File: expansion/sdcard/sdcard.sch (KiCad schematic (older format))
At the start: 26 parts, among them J1 Conn_01x08, J2 Conn_01x10, J3 SD_Card, Q1 2N7002, Q2 2N7002, Q3 2N7002, Q4 2N7002, Q5 2N7002, Q6 2N7002, U1 74HC574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

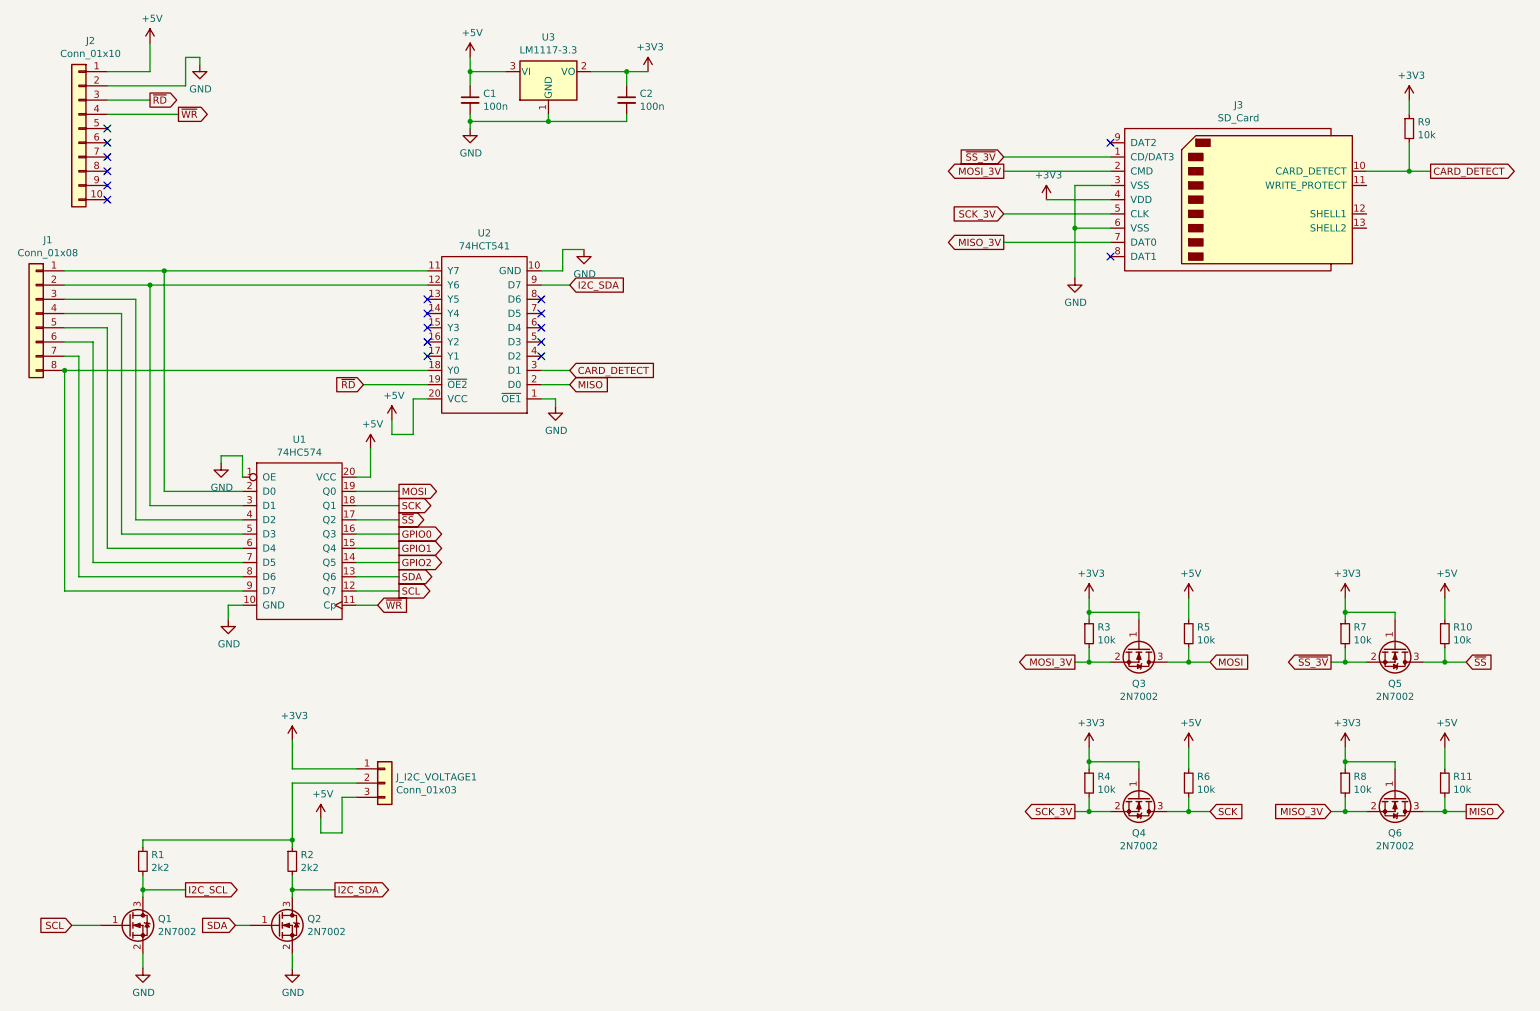
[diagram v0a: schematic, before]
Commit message: SDCard expansion updated.
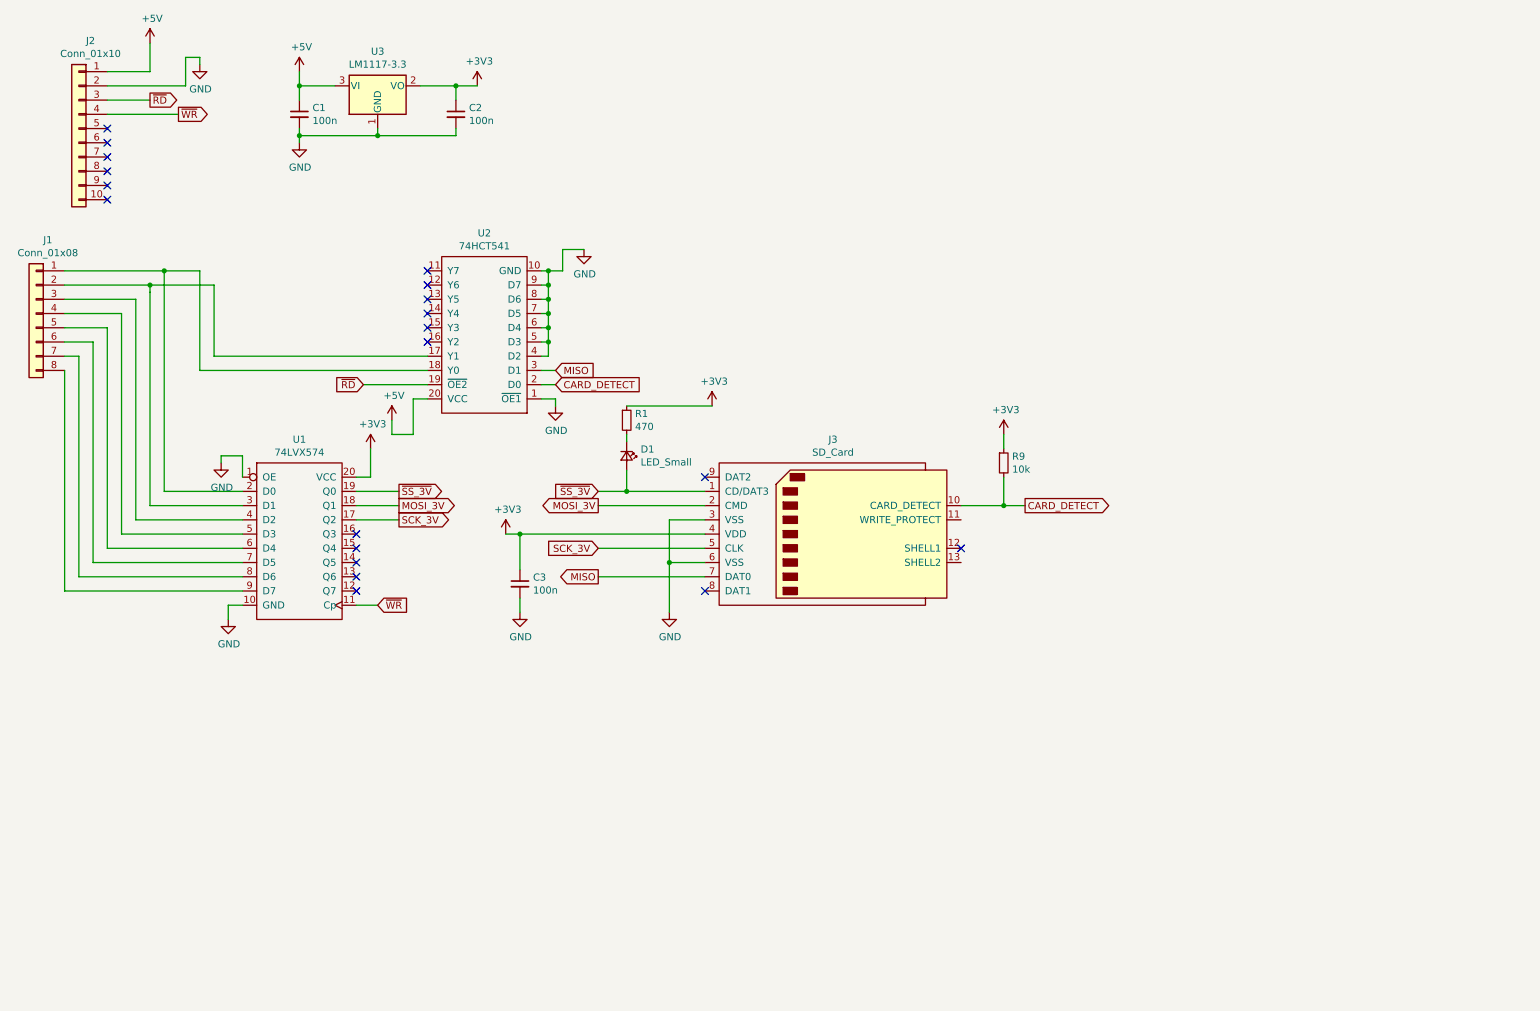
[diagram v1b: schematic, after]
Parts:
- removed J_I2C_VOLTAGE1: Conn_01x03, Connector_PinHeader_2.54mm:PinHeader_1x03_P2.54mm_Vertical, symbol Connector_Generic:Conn_01x03
- removed Q1, Q2, Q3, Q4, Q5, Q6: 2N7002, Package_TO_SOT_SMD:SOT-23, symbol Transistor_FET:2N7002
- removed R10, R11, R3, R4, R5, R6, R7, R8: 10k, Resistor_SMD:R_0805_2012Metric_Pad1.15x1.40mm_HandSolder, symbol Device:R_Small
- removed R2: 2k2, Resistor_SMD:R_0805_2012Metric_Pad1.15x1.40mm_HandSolder, symbol Device:R_Small
- added C3: 100n, Capacitor_SMD:C_0805_2012Metric_Pad1.15x1.40mm_HandSolder, symbol Device:C_Small
- added D1: LED_Small, LED_SMD:LED_0805_2012Metric_Pad1.15x1.40mm_HandSolder, symbol Device:LED_Small
- R1: value 2k2 -> 470
- U1: value 74HC574 -> 74LVX574
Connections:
- net I2C_SDA is gone; now on net GND: U2.9 (D7)
- net MISO_3V is gone; now on net MISO: J3.7 (DAT0)
- net MOSI is gone; now on net ~SS_3V: U1.19 (Q0)
- net SCK is gone; now on net MOSI_3V: U1.18 (Q1)
- net ~SS is gone; now on net SCK_3V: U1.17 (Q2)
- net +3V3: now also R1.1, U1.20 (VCC), C3.1
- net +5V: no longer U1.20 (VCC)
- net CARD_DETECT: now also U2.2 (D0); no longer U2.3 (D1)
- net GND: now also U2.4 (D2), U2.5 (D3), U2.6 (D4), U2.7 (D5), U2.8 (D6), C3.2
- net MISO: now also U2.3 (D1); no longer U2.2 (D0)
- net ~SS_3V: now also D1.2 (A)
- net at J1.1 (Pin_1), U1.2 (D0): now also U2.18 (Y0); no longer U2.11 (Y7)
- net at J1.2 (Pin_2), U1.3 (D1): now also U2.17 (Y1); no longer U2.12 (Y6)
- net at J1.8 (Pin_8), U1.9 (D7): no longer U2.18 (Y0)
- net GPIO0: no longer names the net of U1.16 (Q3)
- net GPIO1: no longer names the net of U1.15 (Q4)
- net GPIO2: no longer names the net of U1.14 (Q5)
- net I2C_SCL: no longer names the net of R1.2
- net I2C_SCL: now also D1.1 (K)
- net SCL: no longer names the net of U1.12 (Q7)
- net SDA: no longer names the net of U1.13 (Q6)
- no-connect marks 18 -> 20
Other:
- moved on the sheet: C1, C2, J3, R9, U3
